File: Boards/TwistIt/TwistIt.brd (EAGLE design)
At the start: 39.9 x 54.8 mm, 21 parts

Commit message: rev a is a gogo
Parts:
- moved BR1 54.4 mm to (-9.13, 19.7)
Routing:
- net CS: track 10.9 -> 35.7 mm
- net INB: track 17.8 -> 36.0 mm
- net INA: track 14.2 -> 32.5 mm
- net VCC: track 78.4 -> 92.3 mm
- net PWM: track 30.8 -> 35.1 mm
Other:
- board size 39.9 x 54.8 mm -> 36.4 x 54.8 mm
- board text added: "TwistIt! Rev 10A"
- board text removed: "TwistIt! Prod"
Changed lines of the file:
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@@
 <board>
 <plain>
-<wire x1="0" y1="0" x2="39.878" y2="0" width="0" layer="20"/>
-<wire x1="39.878" y1="0" x2="39.878" y2="54.788" width="0" layer="20"/>
-<wire x1="39.878" y1="54.788" x2="0" y2="54.788" width="0" layer="20"/>
+<wire x1="0" y1="0" x2="36.4" y2="0" width="0" layer="20"/>
+<wire x1="36.4" y1="0" x2="36.4" y2="54.788" width="0" layer="20"/>
+<wire x1="36.4" y1="54.788" x2="0" y2="54.788" width="0" layer="20"/>
 <wire x1="0" y1="54.788" x2="0" y2="0" width="0" layer="20"/>
 <text x="32.965" y="0.767" size="0.762" layer="25" font="vector" align="center">VCC</text>
@@
 <wire x1="0.427" y1="29.929" x2="3.724" y2="29.924" width="0.1" layer="21"/>
 <text x="19.63" y="50.53" size="1.778" layer="21" font="vector" ratio="15" align="center">TwistIt!
-Prod</text>
+Rev 10A</text>
 <text x="7.223" y="43.588" size="0.6096" layer="25" font="vector" rot="SR270">Vcc</text>
 <text x="7.143" y="40.971" size="0.6096" layer="25" font="vector" rot="SR270">GND</text>
@@
 <attribute name="PACKAGE" value="R0603" x="7.224" y="30.573" size="1.778" layer="27" rot="R180" display="off"/>
 </element>
-<element name="BR1" library="pie" package="VNH2SP30_MOTOR_CONTROLLER" value="VNH2SP30_MOTOR_CONTROLLER" x="45.105" y="24.424"/>
+<element name="BR1" library="pie" package="VNH2SP30_MOTOR_CONTROLLER" value="VNH2SP30_MOTOR_CONTROLLER" x="-9.133" y="19.7"/>
 </elements>
 <signals>
@@
 <polygon width="0.4064" layer="16">
 <vertex x="0" y="54.61"/>
-<vertex x="39.878" y="54.61"/>
-<vertex x="39.878" y="0"/>
+<vertex x="36.3" y="54.61"/>
+<vertex x="36.3" y="0"/>
 <vertex x="0" y="0"/>
 </polygon>
@@
 <contactref element="ST1" pad="P$1"/>
 <contactref element="BR1" pad="GND"/>
-<wire x1="11.938" y1="36.068" x2="27.178" y2="38.608" width="0" layer="19" extent="1-1"/>
-<wire x1="11.938" y1="33.528" x2="11.938" y2="36.068" width="0" layer="19" extent="1-1"/>
-<wire x1="13.016" y1="5.512865625" x2="1.372" y2="20.072" width="0" layer="19" extent="1-1"/>
-<wire x1="84.065" y1="25.924" x2="13.016" y2="5.512865625" width="0" layer="19" extent="1-1"/>
 </signal>
 <signal name="VCC">
@@
 <contactref element="5V_JUMPER" pad="P$1"/>
 <contactref element="ENCODER" pad="1"/>
-<wire x1="3.201" y1="42.829" x2="7.358" y2="46.986" width="0.4064" layer="16"/>
-<wire x1="7.358" y1="46.986" x2="25.272" y2="46.986" width="0.4064" layer="16"/>
 <contactref element="ST1" pad="P$5"/>
 <contactref element="R8" pad="2"/>
@@
 <wire x1="6.362" y1="39.668" x2="6.362" y2="32.452" width="0.4064" layer="1"/>
 <wire x1="27.178" y1="33.528" x2="28.52" y2="34.87" width="0.4064" layer="1"/>
-<wire x1="30.826" y1="34.87" x2="28.52" y2="34.87" width="0.4064" layer="1"/>
-<wire x1="30.826" y1="41.432" x2="30.826" y2="34.87" width="0.4064" layer="1"/>
+<wire x1="28.52" y1="34.87" x2="30.826" y2="34.87" width="0.4064" layer="1"/>
 <wire x1="33.016" y1="5.512865625" x2="33.016" y2="32.68" width="0.4064" layer="16"/>
 <wire x1="33.016" y1="32.68" x2="30.826" y2="34.87" width="0.4064" layer="16"/>
 <contactref element="BR1" pad="+5V"/>
-<wire x1="30.826" y1="41.432" x2="25.272" y2="46.986" width="0" layer="19" extent="1-16"/>
-<wire x1="86.605" y1="25.924" x2="33.016" y2="5.512865625" width="0" layer="19" extent="1-1"/>
+<wire x1="30.826" y1="34.87" x2="30.826" y2="44.599" width="0.4064" layer="1"/>
+<wire x1="30.826" y1="44.599" x2="32.367" y2="46.14" width="0.4064" layer="1"/>
+<wire x1="32.367" y1="46.14" x2="30.146" y2="48.361" width="0.4064" layer="1"/>
+<wire x1="8.733" y1="48.361" x2="3.201" y2="42.829" width="0.4064" layer="1"/>
+<wire x1="30.146" y1="48.361" x2="8.733" y2="48.361" width="0.4064" layer="1"/>
 </signal>
 <signal name="P1">
@@
 <signal name="EN">
 <contactref element="APM" pad="A3"/>
-<wire x1="27.178" y1="30.988" x2="24.955" y2="30.988" width="0.4064" layer="16"/>
-<wire x1="24.955" y1="30.988" x2="22.184" y2="33.759" width="0.4064" layer="16"/>
-<wire x1="22.184" y1="33.759" x2="22.184" y2="44.97" width="0.4064" layer="16"/>
 <contactref element="BR1" pad="EN"/>
-<wire x1="81.525" y1="25.924" x2="27.178" y2="30.988" width="0" layer="19" extent="1-1"/>
+<wire x1="27.287" y1="46.14" x2="24.974" y2="43.827" width="0.4064" layer="1"/>
+<wire x1="24.974" y1="43.827" x2="24.974" y2="33.02" width="0.4064" layer="1"/>
+<wire x1="24.974" y1="33.02" x2="27.006" y2="30.988" width="0.4064" layer="1"/>
+<wire x1="27.006" y1="30.988" x2="27.178" y2="30.988" width="0.4064" layer="1"/>
 </signal>
 <signal name="CS">
 <contactref element="APM" pad="8"/>
-<wire x1="19.656" y1="23.466" x2="11.938" y2="15.748" width="0.4064" layer="1"/>
 <contactref element="BR1" pad="CS"/>
-<wire x1="78.985" y1="25.924" x2="11.938" y2="15.748" width="0" layer="19" extent="1-1"/>
+<wire x1="24.747" y1="46.14" x2="24.747" y2="44.39026875" width="0.4064" layer="1"/>
+<wire x1="24.747" y1="44.39026875" x2="22.45719375" y2="42.1004625" width="0.4064" layer="1"/>
+<wire x1="22.45719375" y1="42.1004625" x2="22.45719375" y2="26.26719375" width="0.4064" layer="1"/>
+<wire x1="22.45719375" y1="26.26719375" x2="11.938" y2="15.748" width="0.4064" layer="1"/>
 </signal>
 <signal name="INA">
 <contactref element="APM" pad="16"/>
-<wire x1="17.116" y1="25.81" x2="27.178" y2="15.748" width="0.4064" layer="16"/>
 <contactref element="BR1" pad="INA"/>
-<wire x1="76.445" y1="25.924" x2="27.178" y2="15.748" width="0" layer="19" extent="1-1"/>
+<wire x1="22.207" y1="46.14" x2="22.207" y2="20.719" width="0.4064" layer="16"/>
+<wire x1="22.207" y1="20.719" x2="27.178" y2="15.748" width="0.4064" layer="16"/>
 </signal>
 <signal name="INB">
 <contactref element="APM" pad="10"/>
-<wire x1="14.576" y1="25.81" x2="27.178" y2="13.208" width="0.4064" layer="16"/>
 <contactref element="BR1" pad="INB"/>
-<wire x1="73.905" y1="25.924" x2="27.178" y2="13.208" width="0" layer="19" extent="1-1"/>
+<wire x1="19.667" y1="46.14" x2="19.667" y2="20.719" width="0.4064" layer="16"/>
+<wire x1="19.667" y1="20.719" x2="27.178" y2="13.208" width="0.4064" layer="16"/>
 </signal>
 <signal name="PWM">
 <contactref element="APM" pad="9"/>
-<wire x1="13.716" y1="43.302" x2="13.716" y2="14.986" width="0.4064" layer="16"/>
-<wire x1="13.716" y1="14.986" x2="11.938" y2="13.208" width="0.4064" layer="16"/>
 <contactref element="BR1" pad="PMW"/>
-<wire x1="71.365" y1="25.924" x2="11.938" y2="13.208" width="0" layer="19" extent="1-1"/>
+<wire x1="17.127" y1="46.14" x2="17.127" y2="18.397" width="0.4064" layer="16"/>
+<wire x1="17.127" y1="18.397" x2="11.938" y2="13.208" width="0.4064" layer="16"/>
 </signal>
 <signal name="LED1">

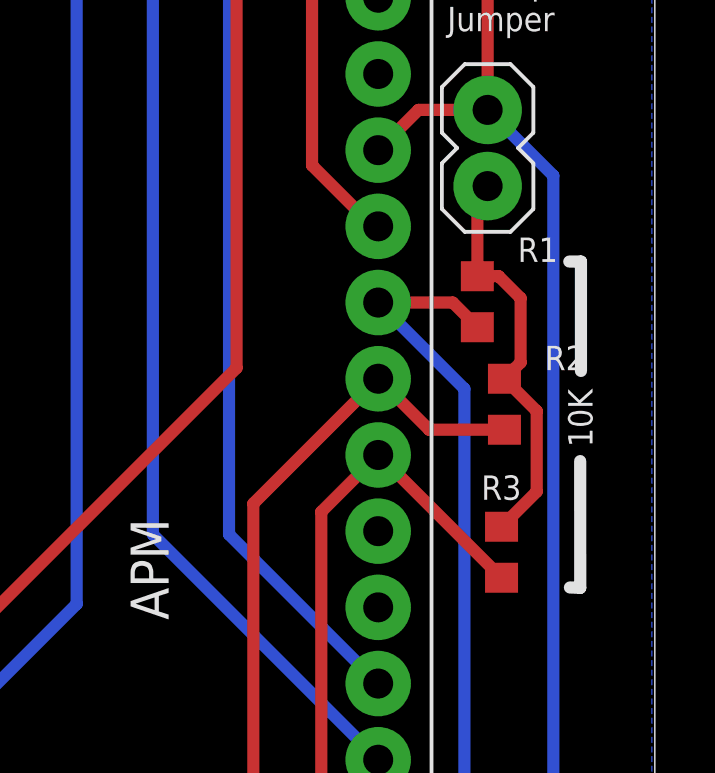
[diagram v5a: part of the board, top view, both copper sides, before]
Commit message: margo altered resistor alignment to please seiya's ocd
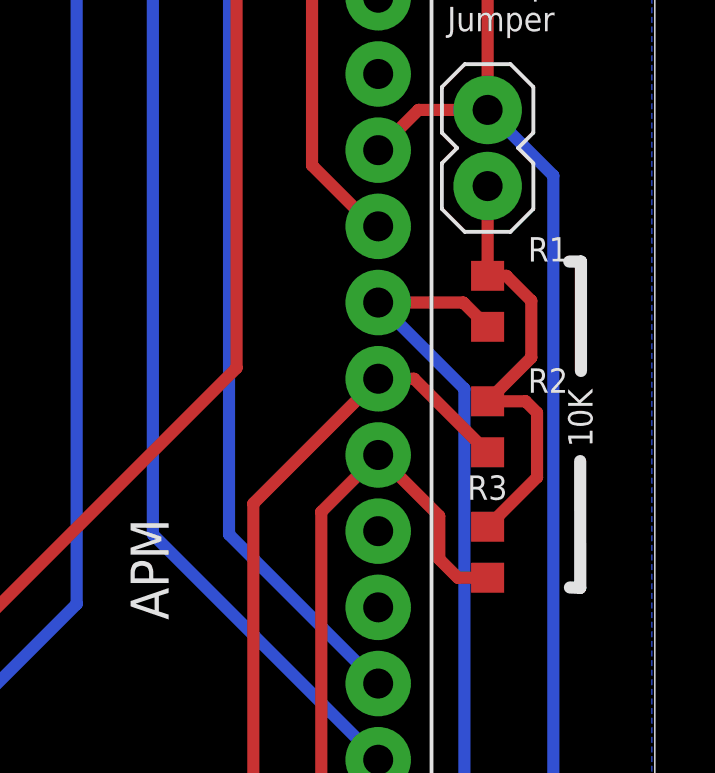
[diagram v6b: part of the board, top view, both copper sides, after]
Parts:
- moved R2 0.94 mm to (30.8, 24.3)
- moved R3 0.46 mm to (30.8, 20.1)
- moved R1 0.34 mm to (30.8, 28.5)
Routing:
- net 5V: track 13.7 -> 15.7 mm
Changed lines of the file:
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@@
 </autorouter>
 <elements>
-<element name="R1" library="resistor" package="R0603" value="10K" x="30.485" y="28.477" smashed="yes" rot="R90">
-<attribute name="NAME" x="33.165509375" y="30.615821875" size="0.8128" layer="25" font="vector" rot="R180"/>
-</element>
-<element name="R2" library="resistor" package="R0603" value="10K" x="31.386" y="25.059" smashed="yes" rot="R90">
-<attribute name="NAME" x="34.064921875" y="27.005515625" size="0.8128" layer="25" font="vector" rot="R180"/>
-</element>
-<element name="R3" library="resistor" package="R0603" value="10K" x="31.29" y="20.124" smashed="yes" rot="R90">
-<attribute name="NAME" x="31.949503125" y="22.685915625" size="0.8128" layer="25" font="vector" rot="R180"/>
+<element name="R1" library="resistor" package="R0603" value="10K" x="30.826" y="28.489" smashed="yes" rot="R90">
+<attribute name="NAME" x="33.506509375" y="30.627821875" size="0.8128" layer="25" font="vector" rot="R180"/>
+</element>
+<element name="R2" library="resistor" package="R0603" value="10K" x="30.826" y="24.307" smashed="yes" rot="R90">
+<attribute name="NAME" x="33.504921875" y="26.253515625" size="0.8128" layer="25" font="vector" rot="R180"/>
+</element>
+<element name="R3" library="resistor" package="R0603" value="10K" x="30.826" y="20.124" smashed="yes" rot="R90">
+<attribute name="NAME" x="31.485503125" y="22.685915625" size="0.8128" layer="25" font="vector" rot="R180"/>
 </element>
 <element name="APM" library="pie" package="ARDUINO_PRO_MICRO" value="ARDUINO_PRO_MICRO" x="10.16" y="11.43">
@@
 <contactref element="R1" pad="2"/>
 <contactref element="5V_JUMPER" pad="P$2"/>
-<wire x1="31.386" y1="25.909" x2="32.462" y2="24.833" width="0.4064" layer="1"/>
-<wire x1="31.386" y1="25.909" x2="31.925" y2="26.448" width="0.4064" layer="1"/>
-<wire x1="31.925" y1="26.448" x2="31.925" y2="28.596" width="0.4064" layer="1"/>
-<wire x1="31.925" y1="28.596" x2="31.194" y2="29.327" width="0.4064" layer="1"/>
-<wire x1="31.194" y1="29.327" x2="30.485" y2="29.327" width="0.4064" layer="1"/>
-<wire x1="32.462" y1="24.833" x2="32.462" y2="22.146" width="0.4064" layer="1"/>
-<wire x1="32.462" y1="22.146" x2="31.29" y2="20.974" width="0.4064" layer="1"/>
-<wire x1="30.485" y1="29.327" x2="30.485" y2="31.989" width="0.4064" layer="1"/>
-<wire x1="30.485" y1="31.989" x2="30.826" y2="32.33" width="0.4064" layer="1"/>
+<wire x1="30.7383125" y1="32.2423125" x2="30.485" y2="31.989" width="0.4064" layer="1"/>
+<wire x1="30.826" y1="32.33" x2="30.7383125" y2="32.2423125" width="0.4064" layer="1"/>
+<wire x1="30.826" y1="32.154625" x2="30.826" y2="29.339" width="0.4064" layer="1"/>
+<wire x1="30.826" y1="32.154625" x2="30.7383125" y2="32.2423125" width="0.4064" layer="1"/>
+<wire x1="32.093" y1="25.157" x2="30.826" y2="25.157" width="0.4064" layer="1"/>
+<wire x1="32.093" y1="25.157" x2="32.474" y2="24.776" width="0.4064" layer="1"/>
+<wire x1="32.474" y1="24.776" x2="32.474" y2="22.622" width="0.4064" layer="1"/>
+<wire x1="32.474" y1="22.622" x2="30.826" y2="20.974" width="0.4064" layer="1"/>
+<wire x1="30.826" y1="25.379" x2="30.826" y2="25.157" width="0.4064" layer="1"/>
+<wire x1="30.826" y1="25.157" x2="32.282" y2="26.613" width="0.4064" layer="1"/>
+<wire x1="32.282" y1="28.509" x2="32.282" y2="26.613" width="0.4064" layer="1"/>
+<wire x1="30.826" y1="29.339" x2="31.452" y2="29.339" width="0.4064" layer="1"/>
+<wire x1="31.452" y1="29.339" x2="32.282" y2="28.509" width="0.4064" layer="1"/>
 </signal>
 <signal name="GND">
@@
 <wire x1="30.052" y1="7.548865625" x2="30.052" y2="25.574" width="0.4064" layer="16"/>
 <wire x1="30.052" y1="25.574" x2="27.178" y2="28.448" width="0.4064" layer="16"/>
-<wire x1="27.178" y1="28.448" x2="29.664" y2="28.448" width="0.4064" layer="1"/>
-<wire x1="29.664" y1="28.448" x2="30.485" y2="27.627" width="0.4064" layer="1"/>
+<wire x1="30.017" y1="28.448" x2="30.826" y2="27.639" width="0.4064" layer="1"/>
+<wire x1="27.178" y1="28.448" x2="30.017" y2="28.448" width="0.4064" layer="1"/>
 </signal>
 <signal name="P2">
@@
 <wire x1="23.016" y1="5.512865625" x2="23.016" y2="21.746" width="0.4064" layer="1"/>
 <wire x1="23.016" y1="21.746" x2="27.178" y2="25.908" width="0.4064" layer="1"/>
-<wire x1="27.178" y1="25.908" x2="28.877" y2="24.209" width="0.4064" layer="1"/>
-<wire x1="28.877" y1="24.209" x2="31.386" y2="24.209" width="0.4064" layer="1"/>
+<wire x1="27.178" y1="25.908" x2="28.375" y2="25.908" width="0.4064" layer="1"/>
+<wire x1="28.375" y1="25.908" x2="30.826" y2="23.457" width="0.4064" layer="1"/>
 </signal>
 <signal name="P3">
@@
 <wire x1="24.592" y1="3.163" x2="25.282" y2="3.853" width="0.4064" layer="1"/>
 <wire x1="25.282" y1="3.853" x2="25.282" y2="21.472" width="0.4064" layer="1"/>
-<wire x1="25.282" y1="21.472" x2="27.178" y2="23.368" width="0.4064" layer="1"/>
-<wire x1="27.178" y1="23.368" x2="27.196" y2="23.368" width="0.4064" layer="1"/>
-<wire x1="27.196" y1="23.368" x2="31.29" y2="19.274" width="0.4064" layer="1"/>
+<wire x1="27.178" y1="23.368" x2="25.282" y2="21.472" width="0.4064" layer="1"/>
+<wire x1="30.826" y1="19.274" x2="29.835" y2="19.274" width="0.4064" layer="1"/>
+<wire x1="29.835" y1="19.274" x2="29.213" y2="19.896" width="0.4064" layer="1"/>
+<wire x1="29.213" y1="19.896" x2="29.213" y2="21.333" width="0.4064" layer="1"/>
+<wire x1="29.213" y1="21.333" x2="27.178" y2="23.368" width="0.4064" layer="1"/>
 </signal>
 <signal name="EN">
